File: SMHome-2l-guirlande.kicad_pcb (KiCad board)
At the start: 2 copper layers, 24.1 x 63.5 mm, 12 parts, among them J1 Screw_Terminal_01x02, SW1 SW_Push, U2 VS1838B, U3 ESP32-C3 Pro Mini, U5 FAN8082

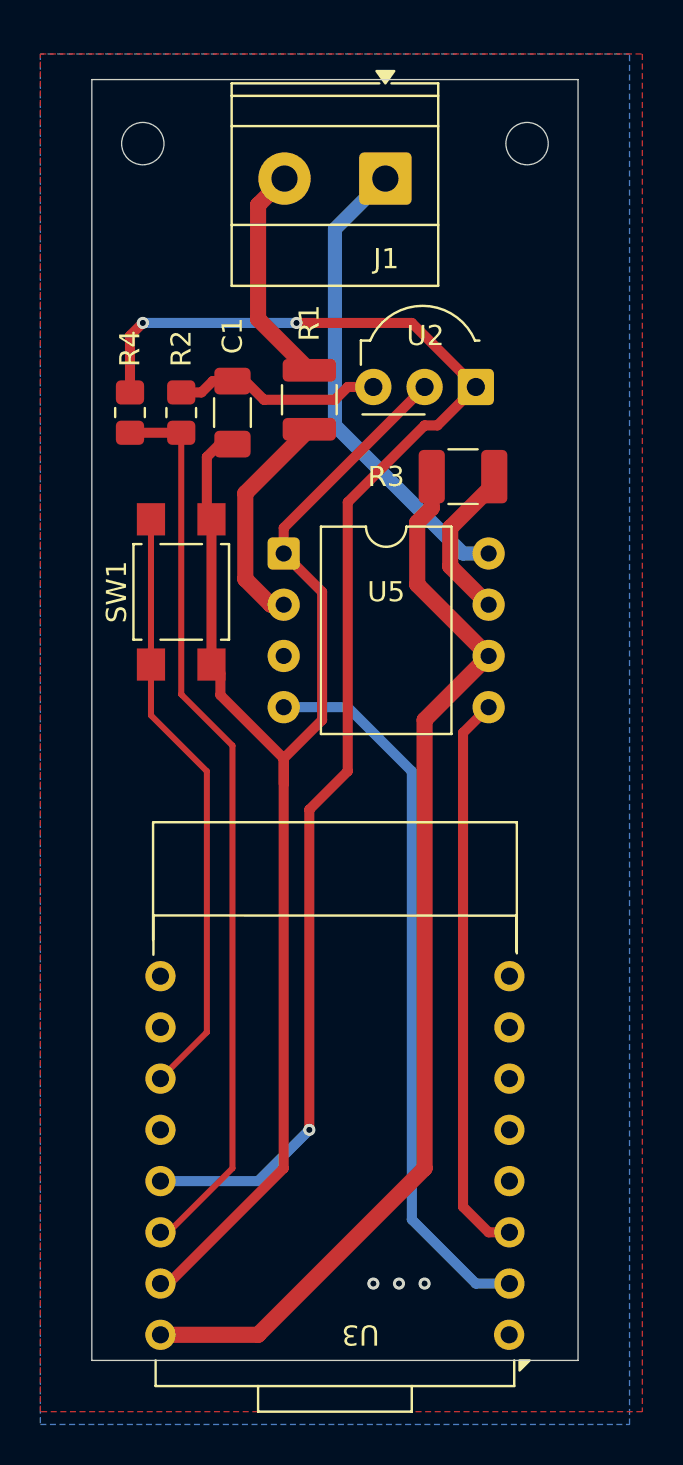
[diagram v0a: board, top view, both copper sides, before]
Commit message: Decrease size. Center BTN
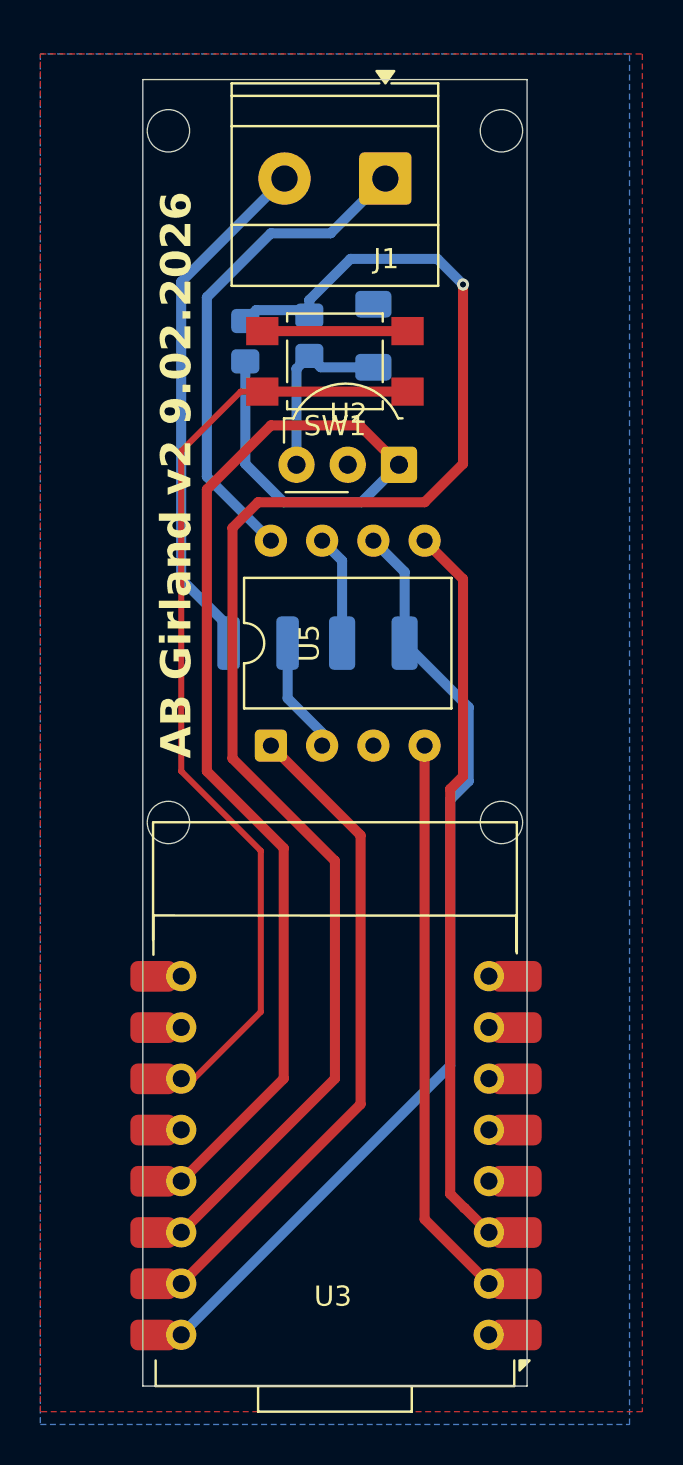
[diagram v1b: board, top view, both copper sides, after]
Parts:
- added TP3: ~, MountingHole:MountingHole_2.1mm, F.Cu at (100.7, 80.2)
- added TP4: ~, MountingHole:MountingHole_2.1mm, F.Cu at (117.2, 80.2)
- C1, R1, R2, R3, R4: moved to B.Cu
- moved SW1 13.7 mm to (109.0, 57.3), turned to 180 degrees
- moved R1 12.3 mm to (105.2, 71.3), turned to 0 degrees
- moved U5 9.55 mm to (105.8, 76.4), turned to 90 degrees
- moved R3 9.38 mm to (110.9, 71.3), turned to 0 degrees
- moved C1 7.96 mm to (110.9, 56.0), turned to 90 degrees
- moved R2 7.41 mm to (107.7, 56.0), turned to -90 degrees
- moved R4 6.72 mm to (104.5, 56.3), turned to 90 degrees
- moved U2 5.42 mm to (112.1, 62.4)
- moved TP1 1.42 mm to (117.2, 45.9)
- moved TP2 1.42 mm to (100.7, 45.9)
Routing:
- net Net-(U3-VCC_3V): track 45.3 -> 76.5 mm, vias 0 -> 1
- net GND: track 71.4 -> 40.8 mm, vias 3 -> 0
- net Net-(U3-GPIO2/A2): track 29.8 -> 48.2 mm
- net Net-(J1-Pin_2): track 11.1 -> 26.6 mm
- net Net-(U3-GPIO6): track 36.0 -> 28.0 mm
- net Net-(U3-GPIO7): track 28.5 -> 36.1 mm
- net +5V: track 54.2 -> 47.2 mm
- net Net-(U2-OUT): track 70.6 -> 63.9 mm, vias 3 -> 0
- net Net-(U5-Vo1): track 11.2 -> 5.79 mm
- net Net-(U5-PVcc): track 8.04 -> 5.49 mm
- net Net-(U2-Vs): track 10.4 -> 9.07 mm
- net Net-(J1-Pin_1): track 23.5 -> 24.7 mm
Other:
- board size 24.1 x 63.5 mm -> 19 x 64.8 mm
- board text added: "AB Girland v2 9.02.2026"
- board text removed: "AB Girland 22.12.2025"

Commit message: Make assemble documents. make narrower
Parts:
- moved TP3 1.27 mm to (100.7, 78.9)
- moved TP4 1.27 mm to (117.2, 78.9)
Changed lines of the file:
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@@
 	(footprint "MountingHole:MountingHole_2.1mm"
 		(layer "F.Cu")
-		(at 100.711 80.1624)
+		(at 100.711 78.8924)
 		(descr "Mounting Hole 2.1mm, no annular, generated by kicad-footprint-generator mountinghole.py")
 		(tags "mountinghole")
@@
 			)
 		)
-		(property "Description" "test point"
+		(property "Description" "Mounting Hole without connection"
 			(at 0 0 0)
 			(layer "F.Fab")
@@
 			)
 		)
-		(property ki_fp_filters "Pin* Test*")
+		(property ki_fp_filters "MountingHole*")
 		(sheetname "/")
 		(sheetfile "SMHome-2l-guirlande.kicad_sch")
-		(attr exclude_from_pos_files)
+		(attr exclude_from_pos_files exclude_from_bom)
 		(fp_circle
 			(center 0 0)
@@
 			)
 		)
-		(property "Description" "test point"
+		(property "Description" "Mounting Hole without connection"
 			(at 0 0 0)
 			(layer "F.Fab")
@@
 			)
 		)
-		(property ki_fp_filters "Pin* Test*")
+		(property ki_fp_filters "MountingHole*")
 		(sheetname "/")
 		(sheetfile "SMHome-2l-guirlande.kicad_sch")
-		(attr exclude_from_pos_files)
+		(attr exclude_from_pos_files exclude_from_bom)
 		(fp_circle
 			(center 0 0)
@@
 		(tags "THT DIP DIL PDIP 2.54mm 10.16mm 400mil")
 		(property "Reference" "U5"
-			(at 5.08 1.905 90)
+			(at 3.175 -0.635 90)
 			(layer "F.SilkS")
 			(effects
@@
 			)
 		)
-		(property "Description" "test point"
+		(property "Description" "Mounting Hole without connection"
 			(at 0 0 0)
 			(layer "F.Fab")
@@
 			)
 		)
-		(property ki_fp_filters "Pin* Test*")
+		(property ki_fp_filters "MountingHole*")
 		(sheetname "/")
 		(sheetfile "SMHome-2l-guirlande.kicad_sch")
-		(attr exclude_from_pos_files)
+		(attr exclude_from_pos_files exclude_from_bom)
 		(fp_circle
 			(center 0 0)
@@
 	(footprint "MountingHole:MountingHole_2.1mm"
 		(layer "F.Cu")
-		(at 117.221 80.1624)
+		(at 117.221 78.8924)
 		(descr "Mounting Hole 2.1mm, no annular, generated by kicad-footprint-generator mountinghole.py")
 		(tags "mountinghole")
@@
 			)
 		)
-		(property "Description" "test point"
+		(property "Description" "Mounting Hole without connection"
 			(at 0 0 0)
 			(layer "F.Fab")
@@
 			)
 		)
-		(property ki_fp_filters "Pin* Test*")
+		(property ki_fp_filters "MountingHole*")
 		(sheetname "/")
 		(sheetfile "SMHome-2l-guirlande.kicad_sch")
-		(attr exclude_from_pos_files)
+		(attr exclude_from_pos_files exclude_from_bom)
 		(fp_circle
 			(center 0 0)
@@
 		)
 		(property "Value" "2R"
-			(at -3.429 0.127 90)
+			(at 0 -1.905 0)
 			(layer "B.Fab")
 			(effects
@@
 		)
 		(property "Value" "100"
-			(at -3.937 0.127 0)
+			(at 0 -1.905 0)
 			(layer "B.Fab")
 			(effects
@@
 		(layer "User.2")
 		(pts
-			(xy 121.031 43.3324) (xy 121.031 106.8324)
+			(xy 118.491 43.3324) (xy 118.491 108.1024)
 		)
 		(height 13.97)
@@
 			(keep_text_aligned yes)
 		)
-		(gr_text "63.5"
-			(at 133.851 75.0824 90)
+		(gr_text "64.77"
+			(at 131.311 75.7174 90)
 			(layer "User.2")
 			(effects
@@
 		(layer "User.2")
 		(pts
-			(xy 96.901 43.3324) (xy 121.031 43.3324)
+			(xy 99.441 43.3324) (xy 118.491 43.3324)
 		)
 		(height -9.525)
@@
 			(keep_text_aligned yes)
 		)
-		(gr_text "24.13"
+		(gr_text "19.05"
 			(at 108.966 32.6574 0)
 			(layer "User.2")
@@
 	)
 	(segment
-		(start 114.681 79.032401)
-		(end 115.596001 78.1174)
+		(start 115.596001 74.4474)
+		(end 112.421001 71.2724)
 		(width 0.5)
 		(layer "B.Cu")
@@
 	)
 	(segment
-		(start 112.421001 67.742401)
-		(end 110.871001 66.192401)
+		(start 115.596001 76.707399)
+		(end 115.596001 74.4474)
 		(width 0.5)
 		(layer "B.Cu")
@@
 	)
 	(segment
-		(start 114.681 92.2274)
-		(end 114.681 79.032401)
+		(start 112.421001 67.742401)
+		(end 110.871001 66.192401)
 		(width 0.5)
 		(layer "B.Cu")
@@
 	)
 	(segment
-		(start 101.346 105.5624)
-		(end 114.681 92.2274)
+		(start 112.421001 71.2724)
+		(end 112.421001 67.742401)
 		(width 0.5)
 		(layer "B.Cu")
@@
 	)
 	(segment
-		(start 112.421001 71.2724)
-		(end 112.421001 67.742401)
+		(start 114.681 77.6224)
+		(end 115.596001 76.707399)
 		(width 0.5)
 		(layer "B.Cu")
@@
 	)
 	(segment
-		(start 115.596001 74.4474)
-		(end 112.421001 71.2724)
+		(start 110.871001 66.192401)
+		(end 110.871 66.192401)
 		(width 0.5)
 		(layer "B.Cu")
@@
 	)
 	(segment
-		(start 110.871001 66.192401)
-		(end 110.871 66.192401)
+		(start 101.346 105.5624)
+		(end 114.681 92.2274)
 		(width 0.5)
 		(layer "B.Cu")
@@
 	)
 	(segment
-		(start 115.596001 78.1174)
-		(end 115.596001 74.4474)
+		(start 114.681 92.2274)
+		(end 114.681 77.6224)
 		(width 0.5)
 		(layer "B.Cu")
@@
 	)
 	(segment
-		(start 101.346 77.6224)
-		(end 101.346 61.7474)
+		(start 101.346 61.7474)
+		(end 104.291 58.8024)
 		(width 0.3)
 		(layer "F.Cu")
@@
 	)
 	(segment
-		(start 101.346 92.8624)
-		(end 101.981 92.8624)
+		(start 101.981 92.8624)
+		(end 105.29 89.5534)
 		(width 0.3)
 		(layer "F.Cu")
@@
 	)
 	(segment
-		(start 101.981 92.8624)
-		(end 105.29 89.5534)
+		(start 105.29 80.9314)
+		(end 101.346 76.9874)
 		(width 0.3)
 		(layer "F.Cu")
@@
 	)
 	(segment
-		(start 105.29 81.5664)
-		(end 101.346 77.6224)
+		(start 105.29 89.5534)
+		(end 105.29 80.9314)
 		(width 0.3)
 		(layer "F.Cu")
@@
 	)
 	(segment
-		(start 105.29 89.5534)
-		(end 105.29 81.5664)
+		(start 101.346 76.9874)
+		(end 101.346 61.7474)
 		(width 0.3)
 		(layer "F.Cu")
@@
 	)
 	(segment
-		(start 101.346 61.7474)
-		(end 104.291 58.8024)
+		(start 101.346 92.8624)
+		(end 101.981 92.8624)
 		(width 0.3)
 		(layer "F.Cu")
@@
 	)
 	(segment
-		(start 106.426 92.8624)
-		(end 106.426 81.4324)
+		(start 101.346 97.9424)
+		(end 106.426 92.8624)
 		(width 0.5)
 		(layer "F.Cu")
@@
 	)
 	(segment
-		(start 106.426 81.4324)
-		(end 102.616 77.6224)
+		(start 106.426 92.8624)
+		(end 106.426 80.7974)
 		(width 0.5)
 		(layer "F.Cu")
@@
 	)
 	(segment
-		(start 110.191 60.4774)
-		(end 112.141 62.4274)
+		(start 102.616 76.9874)
+		(end 102.616 63.6524)
 		(width 0.5)
 		(layer "F.Cu")
@@
 	)
 	(segment
-		(start 102.616 77.6224)
-		(end 102.616 63.6524)
+		(start 106.426 80.7974)
+		(end 102.616 76.9874)
 		(width 0.5)
 		(layer "F.Cu")
@@
 	)
 	(segment
-		(start 101.346 97.9424)
-		(end 106.426 92.8624)
+		(start 110.191 60.4774)
+		(end 112.141 62.4274)
 		(width 0.5)
 		(layer "F.Cu")

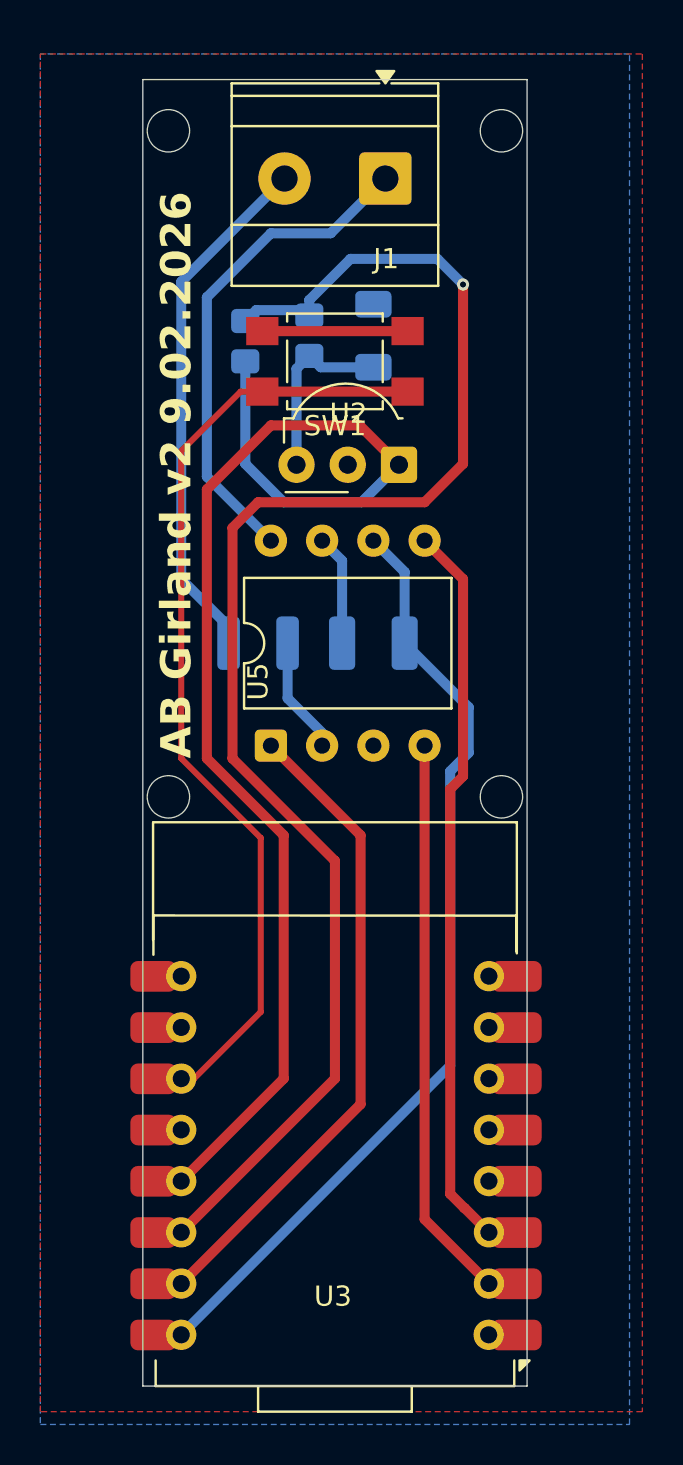
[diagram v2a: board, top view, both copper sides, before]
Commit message: Fix mounting holes. Move sensor
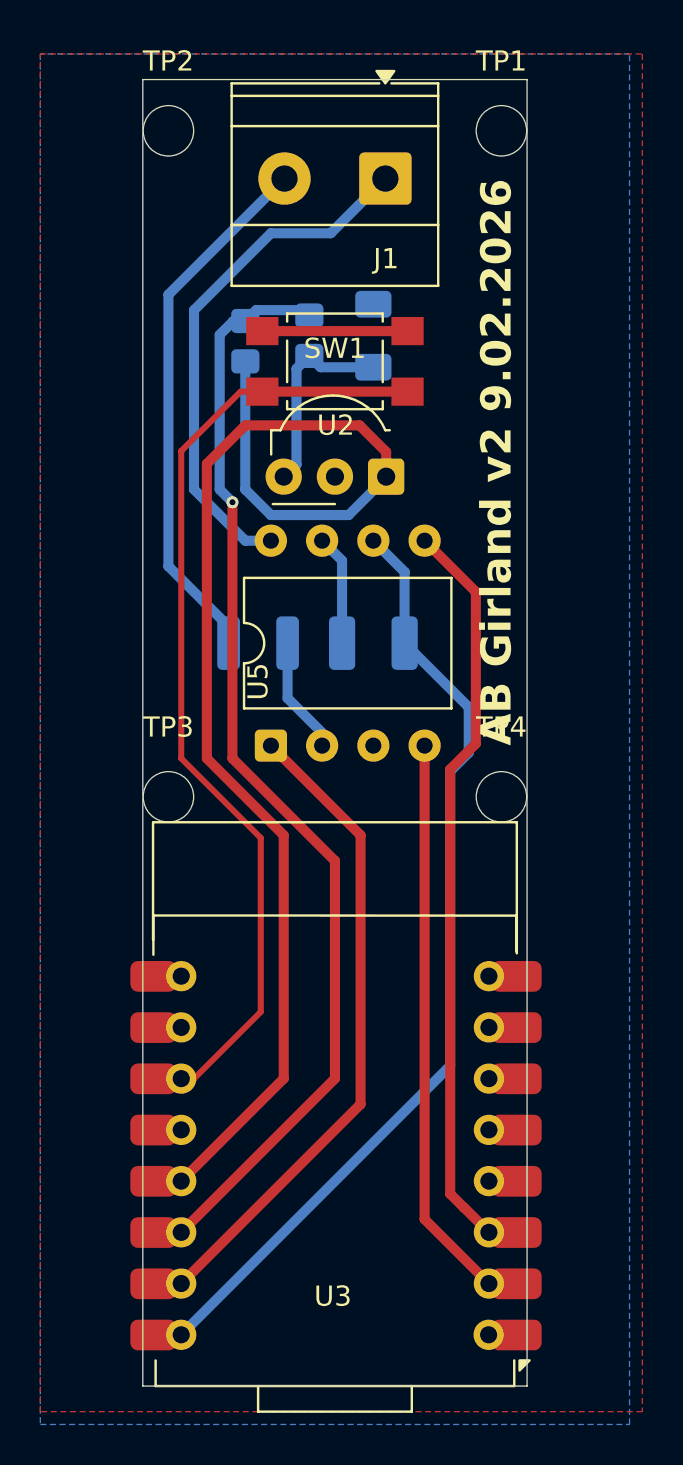
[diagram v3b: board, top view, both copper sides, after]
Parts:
- TP1, TP2, TP3, TP4: footprint MountingHole:MountingHole_2.1mm -> MountingHole:MountingHole_2.5mm
- moved U2 0.87 mm to (111.5, 63.0)
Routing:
- net Net-(U3-VCC_3V): track 76.5 -> 56.5 mm
- net Net-(U2-OUT): track 63.9 -> 65.4 mm
- net Net-(J1-Pin_1): track 24.7 -> 25.9 mm
- net Net-(U2-Vs): track 9.07 -> 9.95 mm
- net Net-(J1-Pin_2): track 26.6 -> 27.1 mm
- net Net-(U3-GPIO7): track 36.1 -> 36.7 mm
